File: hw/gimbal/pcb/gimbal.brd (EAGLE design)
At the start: 68 x 42 mm, 81 parts, among them J1 JST-XH4SMT_RA, J3 JST-XH4SMT_RA, J4 MF-CON-MICROUSB-RIGHT, T12 TPPAD1-13, T3 TPPAD1-13, T8 TPPAD1-13, U1 STM32F4R_64PIN, U2 TPS62172PWSON8, U3 TPS55330PQFN16, U4 MC33926, U5 DRV8313, U6 DRV8313, U7 AS5048A

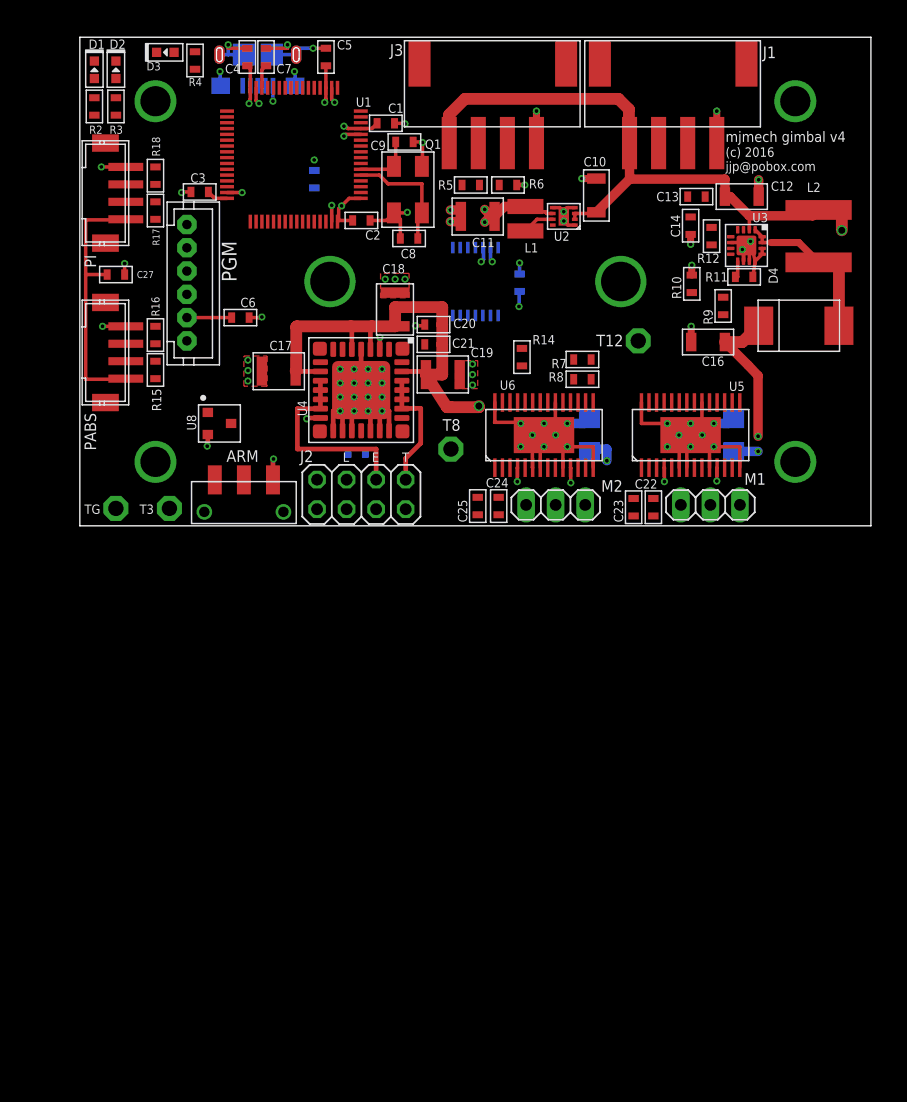
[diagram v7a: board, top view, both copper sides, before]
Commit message: WIP on 18V rs485 version of gimbal board
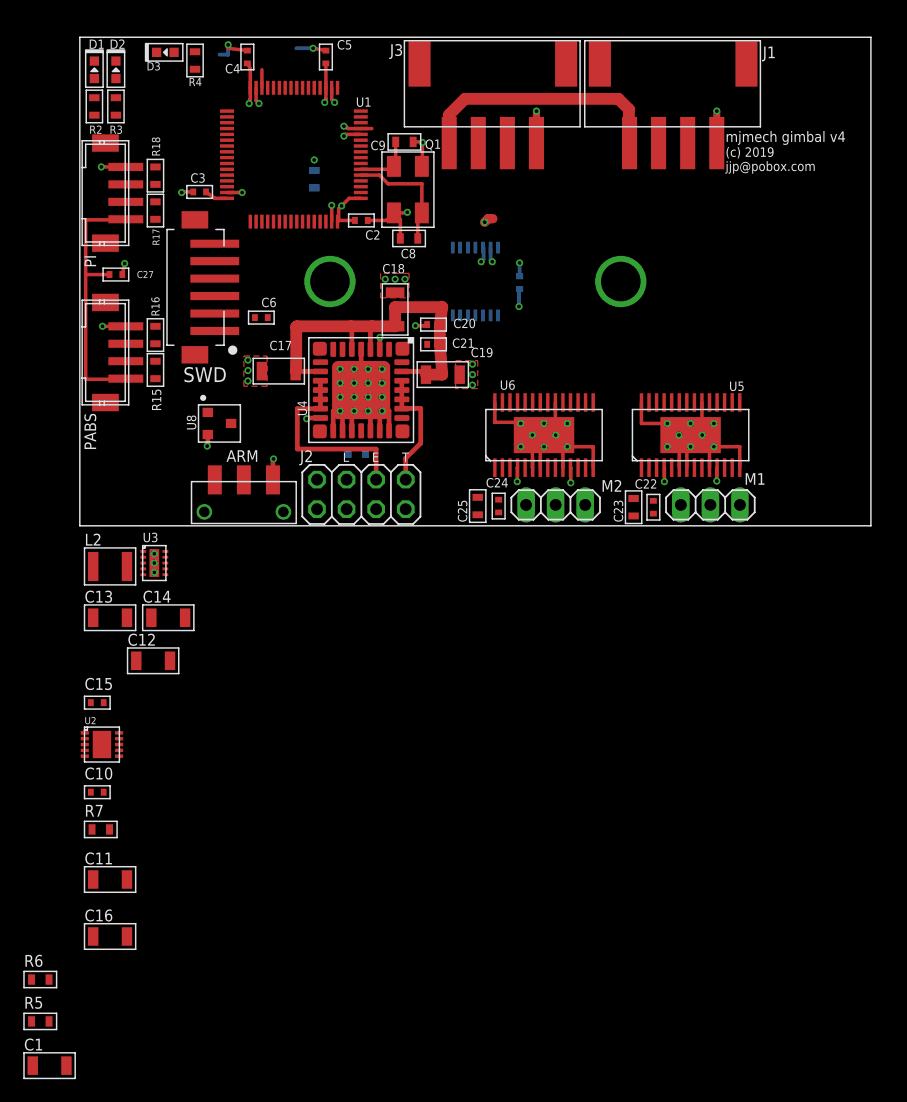
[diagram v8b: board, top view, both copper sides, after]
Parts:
- removed C28, C29: 47uF, rcl:C1206
- removed C7: 4.7uF, mfpassives:C0603
- removed D4: DIODEB520C, gimbal:B520C
- removed J4: MF-CON-MICROUSB-RIGHT, mf_connectors:MICROUSB-RIGHT
- removed L1: 2.2uH, gimbal:L_SMT_1212
- removed PGM: JST-PH6JST-PH6, gimbal:JST-PH6
- removed R10, R8: 10k, mfpassives:R0603
- removed R11: 78.7k, mfpassives:R0603
- removed R12: 1.87k, mfpassives:R0603
- removed R14: 220, mfpassives:R0603
- removed R9: 88.7k, mfpassives:R0603
- removed T12, T3, T8, TG: TPPAD1-13, testpad:P1-13
- removed U$52, U$53, U$54, U$55: M2.5MOUNT, joule_shield:M2.5MOUNT
- added C15: 0.1uF 50V, mfpassives:C0402
- added SWD: JST-ZH6SMT_VERT, controller:JST_B6B-ZR-SM4-TF(LF)(SN)
- C1: value 4.7uF -> 10uF 35V; device mfpassives:C0603 -> mfpassives:C1206
- C10: value 10uF -> 0.1uF 50V; device mfpassives:C1206 -> mfpassives:C0402
- C11, C17, C18, C19: value 22uF 16V -> 10uF 35V; device mfpassives:C1210 -> mfpassives:C1206
- C12, C16: value 10uF -> 10uF 35V
- C13: value 0.047uF -> 10uF 35V; device mfpassives:C0603 -> mfpassives:C1206
- C14: value 0.1uF -> 10uF 35V; device mfpassives:C0603 -> mfpassives:C1206
- C2, C20, C21, C22, C24, C26, C27, C3, C4, C5, C6: value 0.1uF -> 0.1uF 50V; device mfpassives:C0603 -> mfpassives:C0402
- L2: value 2.2uH -> 10uH; device gimbal:ASPI-6045S -> mfpassives:L1210
- R1: value 10 -> 560
- R13, R5: value 100k -> 18k
- R6: value 10k -> 1.69k
- R7: value 100k -> 560
- U2: value TPS62172PWSON8 -> MAX13431E; device gimbal:PWSON8 -> controller:TDFN10
- U3: value TPS55330PQFN16 -> TPS62177WSON10; device gimbal:PQFN16 -> imu_junction:WSON10
- moved C1 86.0 mm to (-2.60, -46.4)
- moved R5 80.9 mm to (-3.40, -42.6), turned to 0 degrees
- moved R6 79.3 mm to (-3.40, -39.0), turned to 0 degrees
- moved C16 72.5 mm to (2.60, -35.3), turned to 0 degrees
- moved L2 67.2 mm to (2.60, -3.50), turned to 0 degrees
- moved C10 66.9 mm to (1.50, -22.9), turned to 0 degrees
- moved C11 65.2 mm to (2.60, -30.4), turned to 0 degrees
- moved C12 64.4 mm to (6.30, -11.6)
- moved C13 62.1 mm to (2.60, -7.90), turned to 0 degrees
- moved U2 60.3 mm to (1.90, -18.8), turned to 0 degrees
- moved R7 57.8 mm to (1.80, -26.1)
- moved U3 57.8 mm to (6.40, -3.20), turned to 0 degrees
- moved C14 56.1 mm to (7.60, -7.90), turned to 0 degrees
- moved C6 1.80 mm to (15.6, 17.9)
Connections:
- removed net +12V: C16.P$1, C22.P$1, C24.P$1, C28.1, C29.1, D4.1, R7.P$2, R9.P$2, T12.TP, U5.11, U5.4, U6.11, U6.4
- removed net BOOST_EN: U1.11, U3.3
- removed net N$16: L1.P$1, U2.7
- removed net N$17: D4.2, L2.2, U3.1, U3.15, U3.16
- removed net N$18: R11.P$2, U3.9
- removed net N$19: C14.P$1, R12.P$1
- removed net N$20: R12.P$2, U3.7
- removed net N$21: C13.P$1, U3.4
- removed net N$22: R10.P$2, R9.P$1, U3.8
- removed net N$38: R7.P$1, R8.P$2, U1.10
- removed net SIMU_SCL: U1.29
- removed net SIMU_SDA: U1.62
- removed net USB_DM: J4.2, U1.44
- removed net USB_DP: J4.3, U1.45
- removed net USB_VBUS: J4.1, U1.42
- new net D1_N: J1.3, J3.3, U2.9
- new net D1_P: J1.2, J3.2, U2.8
- new net DIR3: U2.3, U2.4
- new net N$4: L2.P$1, U3.9
- net +3V3: now also C10.P$1, C13.P$1, C14.P$1, C15.P$1, L2.P$2, SWD.6, U2.1, U2.10, U3.10, U3.8; no longer C1.P$1, C11.P$1, L1.P$2, PGM.6, T3.TP, U2.6
- net +8V: now also C11.P$1, C16.P$1, C22.P$1, C24.P$1, U3.3, U5.11, U5.4, U6.11, U6.4; no longer C10.P$1, L2.1, T8.TP, U2.2, U2.3
- net GND: now also C15.P$2, R7.P$1, SWD.4, U2.6, U2.PAD, U3.1, U3.4, U3.5, U3.P0, U3.P1, U3.P2, U3.P3; no longer C28.2, C29.2, C7.P$2, J4.5, J4.S1, J4.S2, J4.S3, J4.S4, J4.S5, J4.S6, PGM.4, R10.P$1, R11.P$1, R14.P$1, R8.P$1, TG.TP, U2.1, U2.4, U2.5, U2.G0, U2.G1, U2.G2, U3.10, U3.11, U3.12, U3.13, U3.14, U3.G0, U3.G1, U3.G2
- net MOTOR_FB: now also R7.P$2; no longer R14.P$2
- net N$23: now also C1.P$1; no longer C7.P$1
- net N$24: now also SWD.2; no longer PGM.2
- net N$31: now also SWD.5; no longer PGM.5
- net N$32: now also SWD.3; no longer PGM.3
- net SLAVE_RX: now also U2.2; no longer J1.3, J3.3
- net SLAVE_TX: now also U2.5; no longer J1.2, J3.2
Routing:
- net +8V: track 141.1 -> 67.7 mm, vias 2 -> 4
- net +12V: track 52.4 -> 0.00 mm, vias 7 -> 0
- net GND: track 131.9 -> 94.0 mm, vias 44 -> 30
- net N$17: track 14.1 -> 0.00 mm
- net +3V3: track 50.8 -> 44.5 mm, vias 10 -> 9
- net N$24: track 3.85 -> 0.00 mm
- net N$16: track 2.76 -> 0.00 mm
- net N$18: track 1.55 -> 0.00 mm
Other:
- board text added: "(c) 2019 jjp@pobox.com"
- board text removed: "(c) 2016 jjp@pobox.com"
